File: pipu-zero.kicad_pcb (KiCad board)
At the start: 4 copper layers, 80 x 50.5 mm, 79 parts, among them IC1 BQ25176JDSGR, J1 USB_C_Receptacle_USB2.0_14P, J2 Conn_01x08, J3 Micro_SD_Card_Det1, Q1 NMOS, Q2 NMOS, Q3 NMOS, Q4 NMOS, SW1 SW_Push, SW2 SW_Push, U1 BQ297xy, U2 MCP1640Bx-xCHY, U3 MCP1727-0802xSN, U4 ESP32-S3-WROOM-1, U5 CC1101, U6 DM-OLED096-636, U7 TSOP348xx, Y2 Crystal_GND23

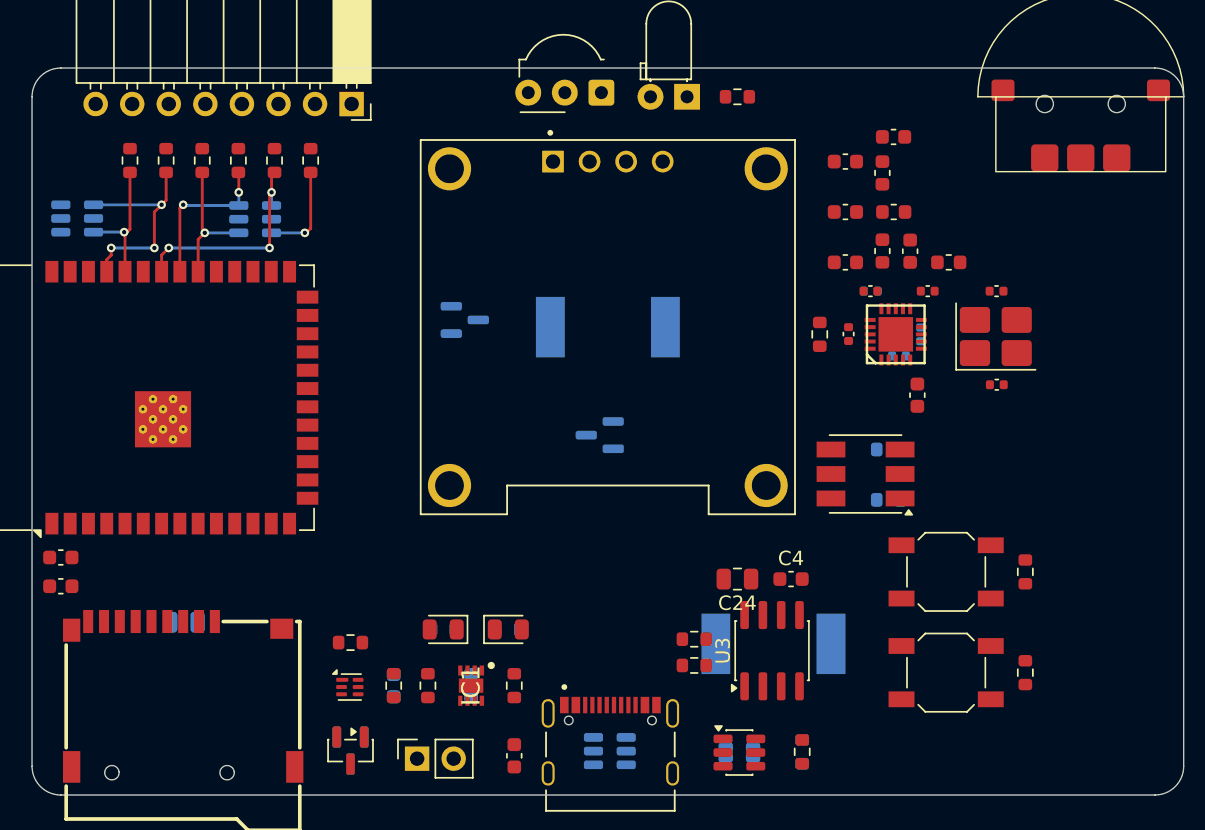
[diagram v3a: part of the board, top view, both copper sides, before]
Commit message: component routing
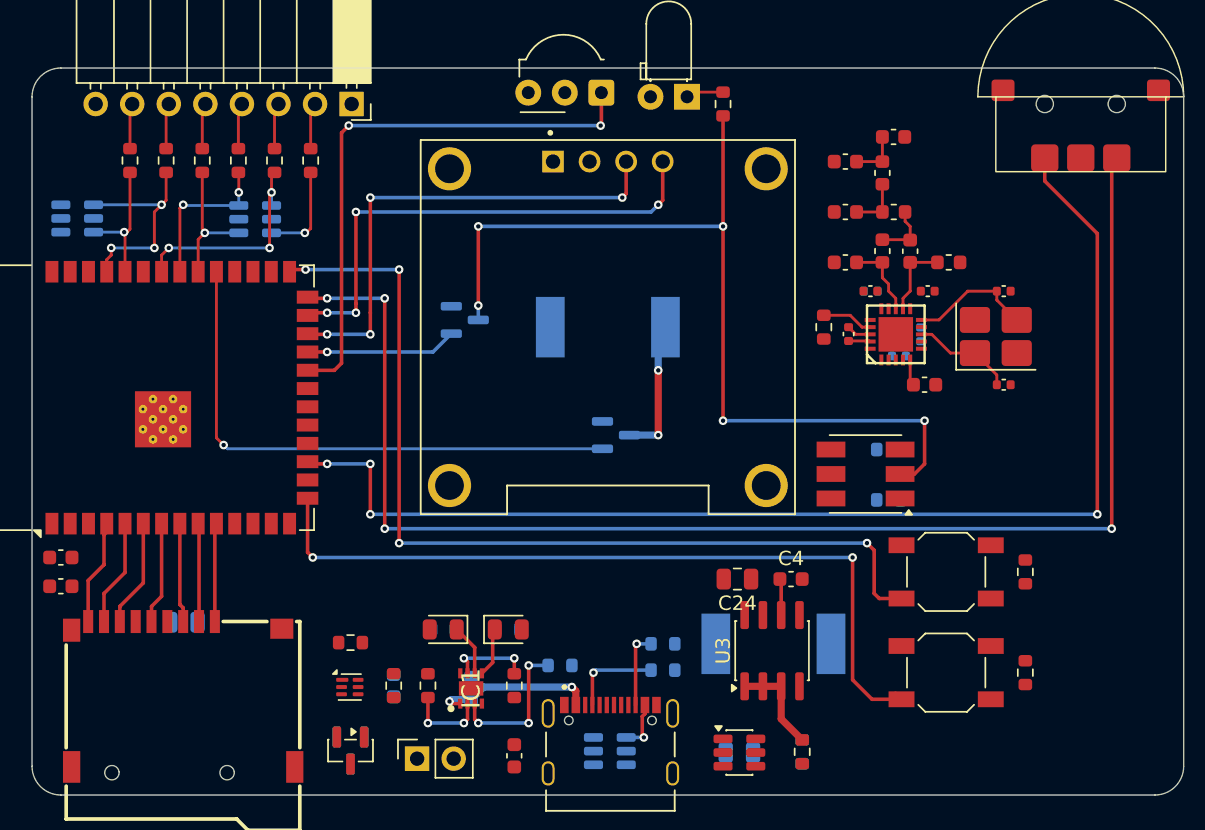
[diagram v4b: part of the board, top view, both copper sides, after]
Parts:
- added R19: R, Resistor_SMD:R_0603_1608Metric, B.Cu at (150.2, 104.0)
- R1, R2: moved to B.Cu
- moved R1 3.06 mm to (157.3, 104.3)
- moved R2 2.64 mm to (157.3, 102.5)
- moved Q3 1.12 mm to (154.1, 88.0), turned to 0 degrees
- moved R11 1.12 mm to (161.5, 65.0), turned to 90 degrees
- moved C11 0.88 mm to (175.5, 84.5), turned to 0 degrees
- moved R12 0.57 mm to (168.5, 80.5)
- moved C15 0.50 mm to (181.0, 78.0)
- moved C14 0.48 mm to (181.0, 84.5)
- moved C1 0.19 mm to (144.0, 105.6), turned to 90 degrees
- moved IC1 0.19 mm to (144.0, 105.6), turned to 90 degrees
- turned R23 to 180 degrees
- turned R4 to 90 degrees
- turned R8 to -90 degrees
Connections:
- net Net-(Q4-G) renamed /MCU/LUIGI
- Q4 pad 3: /I-O/RGB_B -> /I-O/RGB_R
- R11 pad 1: /I-O/RGB_B -> /I-O/RGB_R
- U4 pad 10: /I-O/RGB_R -> /I-O/SD_DAT2
- U4 pad 12: /I-O/SD_CLK -> /I-O/RGB_B
- U4 pad 38: /I-O/SD_CMD -> /MCU/CC1101_GDO2
- U4 pad 39: /I-O/SD_DAT3 -> /MCU/CC1101_GDO0
- U4 pad 4: /I-O/SD_DAT0 -> /I-O/SD_DET
- U4 pad 6: /I-O/SD_DET -> /I-O/SD_DAT0
- U4 pad 7: /I-O/SD_DAT2 -> /I-O/SD_CLK
- U4 pad 8: /MCU/CC1101_GDO2 -> /I-O/SD_CMD
- U4 pad 9: /MCU/CC1101_GDO0 -> /I-O/SD_DAT3
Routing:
- net /I-O/ENCODER_B: track 0.00 -> 97.8 mm, vias 0 -> 4
- net /I-O/ENCODER_A: track 0.00 -> 84.7 mm, vias 0 -> 4
- net /I-O/BTN1: track 0.00 -> 64.9 mm, vias 0 -> 4
- net /I-O/RGB_B: track 0.00 -> 63.7 mm, vias 0 -> 5
- net /I-O/BTN2: track 0.00 -> 54.8 mm, vias 0 -> 2
- net /Infrared/IR_RX: track 0.00 -> 39.1 mm, vias 0 -> 2
- net /I-O/BUZZER: track 0.00 -> 38.7 mm, vias 0 -> 1
- net /I-O/OLED_SDA: track 0.00 -> 34.8 mm, vias 0 -> 4
- net /I-O/OLED_SCL: track 0.00 -> 34.0 mm, vias 0 -> 4
- net /USB_VBUS: track 0.00 -> 14.9 mm, vias 0 -> 3
- net /MCU/LUIGI: track 0.00 -> 10.5 mm, vias 0 -> 1
- net /Power Manager/BAT_NTC: track 0.00 -> 10.3 mm, vias 0 -> 3
- net Net-(BZ1--): track 0.00 -> 9.71 mm, vias 0 -> 2
- net /Radio/XOSC_Q2: track 0.00 -> 8.64 mm
- net /I-O/SD_DAT0: track 0.00 -> 7.48 mm
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
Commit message: routing
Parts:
- moved Q1 56.2 mm to (190.9, 99.4)
- moved Q2 56.2 mm to (190.9, 99.4)
- moved R7 44.7 mm to (179.8, 95.5)
- moved U1 44.7 mm to (179.8, 99.5)
- moved C2 44.6 mm to (182.8, 99.5), turned to 0 degrees
- moved R3 44.6 mm to (182.8, 99.5), turned to 180 degrees
- moved BT1 44.4 mm to (183.8, 102.0)
- moved C3 34.8 mm to (180.8, 102.0), turned to -90 degrees
- moved C1 33.2 mm to (177.0, 109.5)
- moved D3 31.2 mm to (172.5, 108.5)
- moved R8 28.8 mm to (175.5, 109.5)
- moved R4 25.1 mm to (165.5, 111.0)
- moved IC1 25.1 mm to (168.5, 111.0)
- moved R6 23.5 mm to (164.5, 108.5)
- moved R19 23.3 mm to (172.5, 110.5)
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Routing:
- net /I-O/IO41: track 15.2 -> 0.00 mm, vias 3 -> 0
- net /I-O/TXD0: track 15.1 -> 0.84 mm, vias 3 -> 0
- net /I-O/IO40: track 10.9 -> 0.00 mm, vias 2 -> 0
- net /Power Manager/BAT_NTC: track 10.3 -> 0.00 mm, vias 3 -> 0
- net /USB_VBUS: track 14.9 -> 4.96 mm, vias 3 -> 2
- net /I-O/IO39: track 9.53 -> 0.00 mm, vias 1 -> 0
- net /I-O/RXD0: track 9.33 -> 0.00 mm, vias 1 -> 0
- net /I-O/BTN2: track 54.8 -> 46.0 mm
- net /I-O/BTN1: track 64.9 -> 56.2 mm
- net /I-O/IO42: track 6.74 -> 0.00 mm, vias 1 -> 0
- net Net-(IC1-VSET): track 5.73 -> 0.00 mm, vias 2 -> 0
- net Net-(IC1-ISET): track 5.73 -> 0.00 mm, vias 2 -> 0
- net Net-(D3-K): track 3.57 -> 0.00 mm
- net Net-(D2-K): track 3.42 -> 0.00 mm
- net /I-O/IO42_EXT: track 3.23 -> 0.00 mm
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
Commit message: add power supply gaza strip
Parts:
- C1, C2, C23, R10, R19: moved to F.Cu
- C3: moved to B.Cu
- moved D1 42.4 mm to (185.4, 110.0)
- moved J1 42.4 mm to (185.4, 111.6)
- moved R1 42.4 mm to (189.1, 104.4)
- moved R2 42.4 mm to (189.1, 102.6)
- moved Q1 30.0 mm to (163.2, 111.1), turned to 180 degrees
- moved Q2 30.0 mm to (163.2, 111.1), turned to 180 degrees
- moved R7 21.0 mm to (162.7, 107.6), turned to -90 degrees
- moved BT1 18.5 mm to (167.4, 110.7)
- moved R3 16.9 mm to (168.3, 108.2)
- moved U1 16.7 mm to (165.2, 107.6), turned to 90 degrees
- moved C2 16.2 mm to (168.3, 106.7)
- moved D2 15.4 mm to (177.8, 109.2), turned to -90 degrees
- moved C24 15.2 mm to (144.5, 111.8), turned to 0 degrees
- moved R22 14.2 mm to (186.2, 97.4)
- moved SW2 14.2 mm to (180.7, 97.4)
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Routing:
- net /Power Manager/BAT+: track 0.00 -> 43.4 mm, vias 0 -> 1
- net /USB_VBUS: track 4.96 -> 27.9 mm, vias 2 -> 4
- net Net-(BT1--): track 0.00 -> 18.6 mm
- net GND: track 1.52 -> 15.7 mm, vias 0 -> 13
- net /I-O/BTN2: track 46.0 -> 51.6 mm
- net Net-(Q2-G): track 0.00 -> 4.64 mm
- net Net-(U1-BAT): track 0.00 -> 4.61 mm
- net Net-(U2-SW): track 0.00 -> 4.37 mm, vias 0 -> 1
- net /Power Manager/BOOST_OUT: track 6.87 -> 11.1 mm
- net Net-(U2-V_{FB}): track 0.00 -> 3.52 mm
- net Net-(Q1-G): track 0.00 -> 3.39 mm, vias 0 -> 1
- net +3V3: track 1.71 -> 4.98 mm
- net Net-(U3-Cdelay): track 2.54 -> 5.35 mm
- net Net-(D2-A): track 0.00 -> 2.55 mm, vias 0 -> 1
- net Net-(U1-V-): track 0.00 -> 2.10 mm
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
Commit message: giovanni
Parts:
- moved R22 7.47 mm to (190.0, 91.0)
- moved SW2 7.47 mm to (184.5, 91.0)
- moved D4 6.55 mm to (152.4, 64.3)
- moved R11 6.55 mm to (154.9, 64.8)
- moved U7 6.55 mm to (146.5, 64.0)
- moved R21 6.41 mm to (180.1, 98.3)
- moved SW1 6.41 mm to (174.6, 98.3)
- moved Q3 3.14 mm to (155.0, 91.0)
- moved D7 3.11 mm to (174.5, 91.0)
- moved R23 3.11 mm to (176.1, 92.8)
- moved R24 3.11 mm to (176.1, 89.3)
- moved R25 3.11 mm to (172.1, 90.1)
- moved C8 2.90 mm to (176.0, 80.7), turned to -90 degrees
- moved BZ1 2.69 mm to (154.5, 78.0)
- moved L3 2.02 mm to (174.6, 74.9)
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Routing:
- net /I-O/ENCODER_A: track 84.7 -> 6.92 mm, vias 4 -> 3
- net /I-O/ENCODER_B: track 97.8 -> 20.9 mm, vias 4 -> 3
- net /MCU/CC1101_GDO0: track 0.00 -> 68.5 mm, vias 0 -> 2
- net /MCU/CC1101_GDO2: track 0.00 -> 66.9 mm, vias 0 -> 2
- net /I-O/RGB_R: track 0.00 -> 64.1 mm, vias 0 -> 3
- net /I-O/RGB_B: track 63.7 -> 0.00 mm, vias 5 -> 0
- net /MCU/CC1101_NCS: track 0.00 -> 53.1 mm, vias 0 -> 2
- net /MCU/CC1101_MISO: track 0.00 -> 46.5 mm, vias 0 -> 2
- net /MCU/CC1101_SCLK: track 0.00 -> 44.5 mm, vias 0 -> 2
- net /MCU/CC1101_MOSI: track 0.00 -> 43.8 mm, vias 0 -> 2
- net GND: track 15.7 -> 50.7 mm, vias 13 -> 37
- net +3V3: track 4.98 -> 25.8 mm, vias 0 -> 15
- net /I-O/IO39: track 0.00 -> 10.4 mm, vias 0 -> 1
- net /I-O/BTN1: track 56.2 -> 66.6 mm
- net /I-O/BTN2: track 51.6 -> 61.2 mm
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
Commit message: finish routing
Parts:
- added JP1: SolderJumper_2_Open, Jumper:SolderJumper-2_P1.3mm_Open_TrianglePad1.0x1.5mm, F.Cu at (192.1, 76.2)
- added JP2: SolderJumper_2_Open, Jumper:SolderJumper-2_P1.3mm_Open_TrianglePad1.0x1.5mm, F.Cu at (188.5, 76.2)
- moved Q4 1.53 mm to (144.2, 81.0)
- moved Q3 1.50 mm to (155.0, 89.5)
- moved R25 1.09 mm to (172.8, 89.2), turned to 180 degrees
- moved BZ1 1.06 mm to (155.2, 77.2), turned to 90 degrees
- moved D1 0.24 mm to (185.5, 110.2), turned to -90 degrees
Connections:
- net /USB_DM renamed /USB_D-
- net /USB_DP renamed /USB_D+
- D5 pad 1: /I-O/IO39 -> /I-O/IO42
- D5 pad 3: /I-O/IO40 -> /I-O/IO41
- D5 pad 4: /I-O/IO41 -> /I-O/IO40
- D5 pad 6: /I-O/IO42 -> /I-O/IO39
- D6 pad 4: /I-O/TXD0 -> /I-O/RXD0
- D6 pad 6: /I-O/RXD0 -> /I-O/TXD0
- J2 pad 2: /I-O/IO42_EXT -> /I-O/IO39_EXT
- J2 pad 3: /I-O/IO41_EXT -> /I-O/IO40_EXT
- J2 pad 4: /I-O/IO40_EXT -> /I-O/IO41_EXT
- J2 pad 5: /I-O/IO39_EXT -> /I-O/IO42_EXT
- J2 pad 6: /I-O/TXD0_EXT -> /I-O/RXD0_EXT
- J2 pad 7: /I-O/RXD0_EXT -> /I-O/TXD0_EXT
- R13 pad 1: /I-O/RXD0 -> /I-O/TXD0
- R13 pad 2: /I-O/RXD0_EXT -> /I-O/TXD0_EXT
- R14 pad 1: /I-O/TXD0 -> /I-O/RXD0
- R14 pad 2: /I-O/TXD0_EXT -> /I-O/RXD0_EXT
- R15 pad 1: /I-O/IO39 -> /I-O/IO42
- R15 pad 2: /I-O/IO39_EXT -> /I-O/IO42_EXT
- R16 pad 1: /I-O/IO40 -> /I-O/IO41
- R16 pad 2: /I-O/IO40_EXT -> /I-O/IO41_EXT
- R17 pad 1: /I-O/IO41 -> /I-O/IO40
- R17 pad 2: /I-O/IO41_EXT -> /I-O/IO40_EXT
- R18 pad 1: /I-O/IO42 -> /I-O/IO39
- R18 pad 2: /I-O/IO42_EXT -> /I-O/IO39_EXT
- U8 pad C: /I-O/ENCODER_C -> Net-(JP1-A)
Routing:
- net /I-O/ENCODER_B: track 20.9 -> 106.6 mm, vias 3 -> 4
- net /I-O/ENCODER_C: track 0.00 -> 81.5 mm, vias 0 -> 2
- net /I-O/ENCODER_A: track 6.92 -> 82.7 mm, vias 3 -> 2
- net /USB_D+: track 0.00 -> 67.0 mm, vias 0 -> 1
- net /USB_D-: track 0.00 -> 66.2 mm, vias 0 -> 1
- net /I-O/RGB_B: track 0.00 -> 63.1 mm, vias 0 -> 4
- net /I-O/RGB_G: track 0.00 -> 60.2 mm, vias 0 -> 2
- net Net-(JP1-A): track 0.00 -> 31.4 mm
- net Net-(BZ1--): track 2.83 -> 17.8 mm
- net /I-O/IO42: track 2.98 -> 15.3 mm
- net /I-O/IO40: track 4.14 -> 12.9 mm
- net /I-O/IO41: track 3.68 -> 11.1 mm
- net GND: track 50.7 -> 57.3 mm, vias 37 -> 41
- net /I-O/RXD0: track 2.52 -> 5.95 mm
- net /I-O/TXD0: track 2.45 -> 5.80 mm
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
